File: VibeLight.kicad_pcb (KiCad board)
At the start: 2 copper layers, 61.1 x 36.9 mm, 17 parts, among them SW1 SW_Push, SW2 SW_Push, U2 ADXL343, U3 BL652, U4 LK112M33TR

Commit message: started work on pcb layout
started work on pcb layout
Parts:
- added C5: C, Capacitor_SMD:C_0603_1608Metric_Pad1.08x0.95mm_HandSolder, F.Cu at (77.1, 43.2)
- added C6: C, Capacitor_SMD:C_0603_1608Metric_Pad1.08x0.95mm_HandSolder, F.Cu at (70.3, 38.1)
- added C7: C, Capacitor_SMD:C_0603_1608Metric_Pad1.08x0.95mm_HandSolder, F.Cu at (66.9, 40.6)
- added D1: LED, LED_SMD:LED_0603_1608Metric_Pad1.05x0.95mm_HandSolder, F.Cu at (59.3, 48.3)
- added Mic1: Here for custom footprint, MEMS_Mic_SMD:Mic_SMD_0603_1608Metric, F.Cu at (78.6, 38.6)
- added R3: R, Resistor_SMD:R_0603_1608Metric_Pad0.98x0.95mm_HandSolder, F.Cu at (46.6, 30.5)
- added R4: R, Resistor_SMD:R_0603_1608Metric_Pad0.98x0.95mm_HandSolder, F.Cu at (52.4, 30.5)
- added R5: R, Resistor_SMD:R_0603_1608Metric_Pad0.98x0.95mm_HandSolder, F.Cu at (70.2, 30.5)
- added R6: R, Resistor_SMD:R_0603_1608Metric_Pad0.98x0.95mm_HandSolder, F.Cu at (72.8, 43.2)
- added U1: AD8603, Package_TO_SOT_SMD:TSOT-23-5, F.Cu at (59.6, 37.1)
- RV3: value Intensity Dial -> Sens Dial
- moved C3 48.7 mm to (28.1, 48.6), turned to -90 degrees
- moved PWR_REG1 46.7 mm to (27.0, 44.6), turned to 90 degrees
- moved Accel1 46.1 mm to (69.9, 21.3), turned to -90 degrees
- moved SW2 38.8 mm to (33.0, 20.3)
- moved SW1 27.2 mm to (24.9, 20.3)
- moved R2 25.1 mm to (22.8, 40.6), turned to 180 degrees
- moved R1 20.3 mm to (27.1, 40.6), turned to 180 degrees
- moved RV3 14.7 mm to (66.0, 47.2), turned to 90 degrees
- moved RV2 14.7 mm to (41.7, 20.3)
- moved C1 13.7 mm to (43.2, 43.2)
- moved C4 10.8 mm to (53.3, 18.6)
- moved Temp1 7.65 mm to (56.6, 20.7), turned to 180 degrees
- moved Re1 7.61 mm to (45.7, 48.3), turned to -90 degrees
- moved C2 6.24 mm to (50.8, 48.3), turned to 90 degrees
- moved Re2 5.21 mm to (49.2, 43.2)
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- renumbered U2 to Accel1, U4 to PWR_REG1
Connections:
- net Intensity_Dial renamed /MCU/Intensity_Dial
- Accel1 pad 13: unconnected-(U2-SDA/SDI/SDIO-Pad13) -> /MCU/SCL
- Accel1 pad 14: unconnected-(U2-SCL/SCLK-Pad14) -> Net-(Accel1-SCL/SCLK)
- Accel1 pad 2: Net-(U2-GND-Pad2) -> GND
- Accel1 pad 4: Net-(U2-GND-Pad2) -> GND
- Accel1 pad 5: Net-(U2-GND-Pad2) -> GND
- Accel1 pad 6: +3V3 -> /Audio Input/PWR
- Accel1 pad 7: unconnected-(U2-~{CS}-Pad7) -> /Audio Input/PWR
- Accel1 pad 8: /ACCEL_INT1 -> /MCU/ACC_INT1
- Accel1 pad 9: /ACCEL_INT2 -> /MCU/ACC_INT2
- C4 pad 1: +3V3 -> /Audio Input/PWR
- PWR_REG1 pad 4: +3V3 -> /Audio Input/PWR
- R1 pad 1: Battery -> /Audio Input/PWR
- RV2 pad 1: +3V3 -> /Audio Input/PWR
- RV2 pad 3: /BATT+ -> GND
- RV3 pad 1: unconnected-(RV3-Pad1) -> /Audio Input/RAW
- RV3 pad 2: /Audio Input/Inverting Input -> Net-(U1--)
- RV3 pad 3: unconnected-(RV3-Pad3) -> GND
- SW1 pad 1: /BATT+ -> /MCU/SW1
- SW1 pad 2: unconnected-(SW1-Pad2) -> /Audio Input/PWR
- SW2 pad 1: /BATT+ -> /MCU/SW2
- SW2 pad 2: unconnected-(SW2-Pad2) -> /Audio Input/PWR
- Temp1 pad 1: unconnected-(Temp1-SDA-Pad1) -> Net-(Accel1-SCL/SCLK)
- Temp1 pad 2: unconnected-(Temp1-SCL-Pad2) -> /MCU/SCL
- Temp1 pad 3: +3V3 -> /Audio Input/PWR
- U3 pad 10: unconnected-(U3-SIO_16-Pad10) -> /MCU/SW2
- U3 pad 2: unconnected-(U3-SIO_24-Pad2) -> /MCU/ACC_INT1
- U3 pad 20: /MCU/Batt_Meas -> unconnected-(U3-SIO_05/AIN3-Pad20)
- U3 pad 22: Audio_RAW -> /Audio Input/RAW
- U3 pad 23: /MCU/Audio_FIL -> /Audio Input/FIL
- U3 pad 26: unconnected-(U3-VDD-Pad26) -> /Audio Input/PWR
- U3 pad 29: unconnected-(U3-SIO_15-Pad29) -> /MCU/SW1
- U3 pad 3: unconnected-(U3-SIO_23-Pad3) -> /MCU/ACC_INT2
- U3 pad 36: unconnected-(U3-SIO_27-Pad36) -> /MCU/LED_CNTRL
- U3 pad 38: unconnected-(U3-SIO_25-Pad38) -> /MCU/Batt_Meas
- U3 pad 4: unconnected-(U3-SIO_22-Pad4) -> /MCU/OPT_INT
- U3 pad 5: /MCU/SWDIO -> /MCU/SCL
- U3 pad 6: /MCU/SWCLK -> /MCU/SCL
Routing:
- net /Audio Input/RAW: track 0.00 -> 54.3 mm
- net /MCU/Intensity_Dial: track 29.5 -> 0.00 mm, vias 2 -> 0
- net /Audio Input/FIL: track 0.00 -> 14.1 mm
- net Net-(U1--): track 0.00 -> 12.5 mm
- net Net-(U1-+): track 0.00 -> 12.2 mm, vias 0 -> 2
- net Net-(C1-Pad2): track 0.00 -> 8.50 mm
- net /MCU/Batt_Meas: track 0.00 -> 5.75 mm
- net /Audio Input/PWR: track 0.00 -> 5.71 mm
- net Net-(C7-Pad2): track 0.00 -> 5.17 mm
- net /BATT+: track 0.00 -> 4.19 mm
- net Net-(D1-A): track 0.00 -> 3.59 mm
- net Net-(PWR_REG1-Bypass): track 0.00 -> 2.14 mm
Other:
- board text added: "LIGHT"

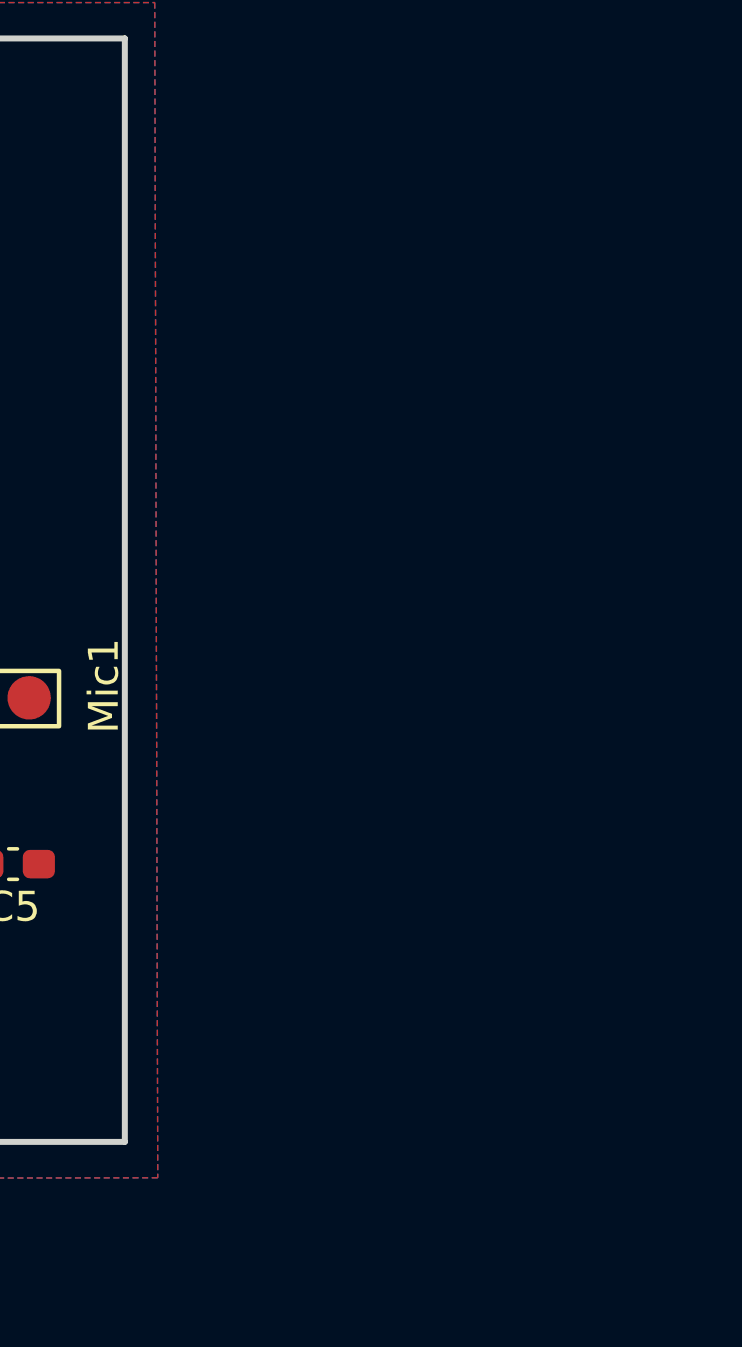
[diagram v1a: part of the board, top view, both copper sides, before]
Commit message: added OPT and JST footprints
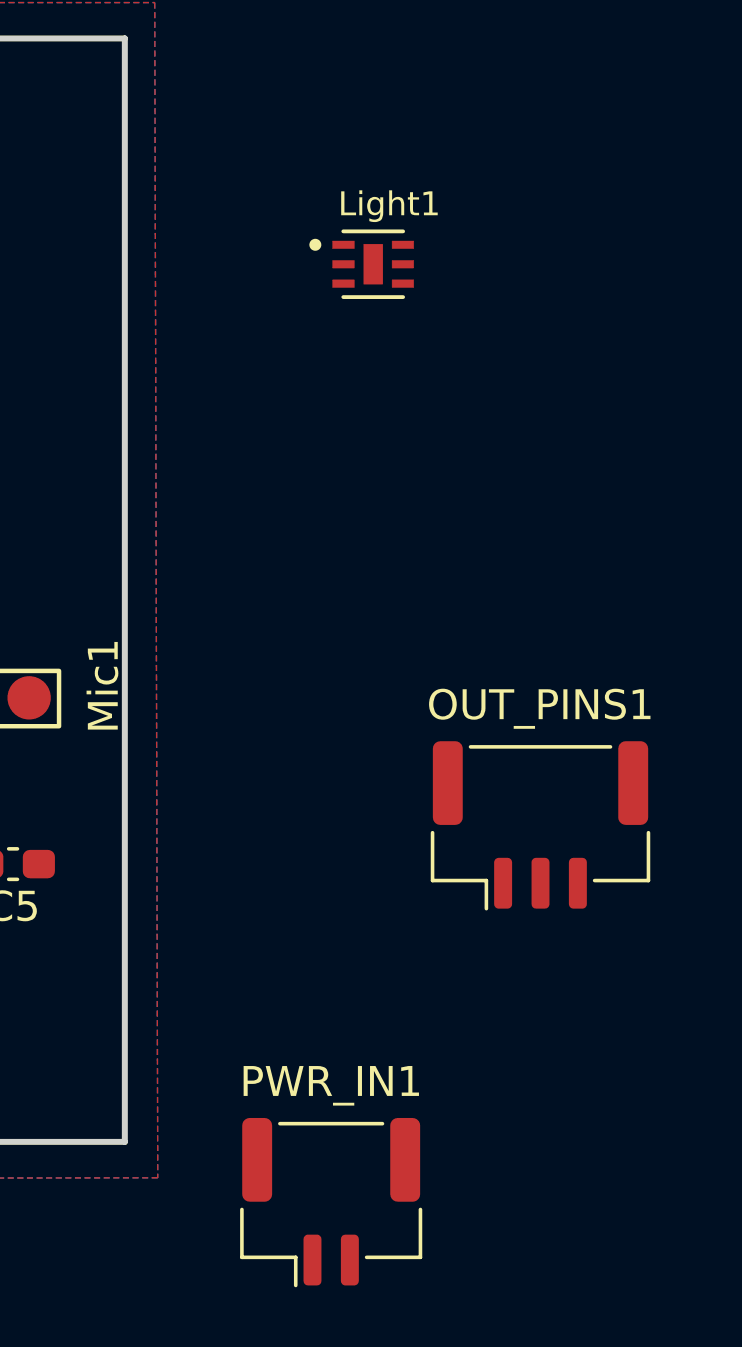
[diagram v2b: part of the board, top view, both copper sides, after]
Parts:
- added Light1: OPT3002-ALS, OP3002:SON65P200X200X65-7N, F.Cu at (89.1, 23.1)
- added OUT_PINS1: Conn_01x03_Pin, Connector_JST:JST_GH_BM03B-GHS-TBT_1x03-1MP_P1.25mm_Vertical, F.Cu at (94.7, 41.9)
- added PWR_IN1: Conn_01x02, Connector_JST:JST_GH_BM02B-GHS-TBT_1x02-1MP_P1.25mm_Vertical, F.Cu at (87.7, 54.5)

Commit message: completed rev1 of PCB layout
need to double check components and other elements, connections, and add values
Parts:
- removed Mic1: Here for custom footprint, MEMS_Mic_SMD:Mic_SMD_0603_1608Metric
- added U2: SPV08A0LR5H-1, MEMS_Mic_SMD:SPV08A0LR5H-1, F.Cu at (77.4, 37.5)
- moved PWR_IN1 63.2 mm to (25.0, 46.4), turned to 90 degrees
- moved OUT_PINS1 27.9 mm to (76.0, 21.2), turned to -90 degrees
- moved Light1 15.0 mm to (77.0, 32.0), turned to 90 degrees
- moved R4 11.4 mm to (41.0, 30.5), turned to 90 degrees
- moved R3 7.63 mm to (39.0, 30.4), turned to 90 degrees
- moved R5 7.23 mm to (77.0, 28.0), turned to -90 degrees
- moved C3 7.01 mm to (35.1, 48.6)
- moved PWR_REG1 7.01 mm to (34.0, 44.6)
- moved R2 7.01 mm to (29.8, 40.6)
- moved R1 7.01 mm to (34.1, 40.6)
- moved Accel1 6.07 mm to (64.0, 20.0)
- moved C4 2.66 mm to (51.0, 19.8)
- moved Temp1 2.66 mm to (54.2, 21.9)
- moved U1 1.85 mm to (59.6, 39.0)
- turned RV2 to -90 degrees
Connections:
- Accel1 pad 13: /MCU/SCL -> /MCU/SDA
- Accel1 pad 14: Net-(Accel1-SCL/SCLK) -> /MCU/SCL
- Light1 pad 6: Net-(Accel1-SCL/SCLK) -> /MCU/SDA
- R3 pad 2: unconnected-(R3-Pad2) -> /MCU/SCL
- R4 pad 2: unconnected-(R4-Pad2) -> /MCU/SDA
- Temp1 pad 1: Net-(Accel1-SCL/SCLK) -> /MCU/SDA
- U3 pad 10: /MCU/SW2 -> unconnected-(U3-SIO_16-Pad10)
- U3 pad 17: unconnected-(U3-SIO_08-Pad17) -> /MCU/ACC_INT1
- U3 pad 18: unconnected-(U3-SIO_07-Pad18) -> /MCU/ACC_INT2
- U3 pad 19: unconnected-(U3-SIO_06-Pad19) -> /MCU/OPT_INT
- U3 pad 2: /MCU/ACC_INT1 -> /MCU/SW1
- U3 pad 21: /MCU/Intensity_Dial -> unconnected-(U3-SIO_04/AIN2-Pad21)
- U3 pad 29: /MCU/SW1 -> unconnected-(U3-SIO_15-Pad29)
- U3 pad 3: /MCU/ACC_INT2 -> /MCU/SW2
- U3 pad 36: /MCU/LED_CNTRL -> unconnected-(U3-SIO_27-Pad36)
- U3 pad 4: /MCU/OPT_INT -> /MCU/Intensity_Dial
- U3 pad 5: /MCU/SCL -> /MCU/SDA
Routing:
- net /Audio Input/PWR: track 5.71 -> 166.4 mm, vias 0 -> 2
- net /MCU/SCL: track 0.00 -> 105.6 mm, vias 0 -> 8
- net /MCU/SDA: track 0.00 -> 94.6 mm, vias 0 -> 8
- net /MCU/OPT_INT: track 0.00 -> 44.6 mm, vias 0 -> 2
- net /MCU/ACC_INT2: track 0.00 -> 32.7 mm, vias 0 -> 2
- net /MCU/ACC_INT1: track 0.00 -> 31.3 mm, vias 0 -> 2
- net /MCU/Intensity_Dial: track 0.00 -> 19.7 mm
- net GND: track 0.00 -> 12.1 mm, vias 0 -> 2
- net /BATT+: track 4.19 -> 9.81 mm
- net /Audio Input/MEMS Mic/2_OUT: track 0.00 -> 5.14 mm
- net /Audio Input/RAW: track 54.3 -> 49.9 mm, vias 0 -> 2
- net /MCU/Batt_Meas: track 5.75 -> 9.03 mm
- net Net-(U1-+): track 12.2 -> 14.6 mm
- net /Audio Input/FIL: track 14.1 -> 15.6 mm, vias 0 -> 2
- net Net-(U1--): track 12.5 -> 12.0 mm
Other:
- board text removed: "LIGHT"

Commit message: Changes from DR call
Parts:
- moved PWR_IN1 62.2 mm to (84.8, 29.1), turned to -90 degrees
- moved PWR_REG1 53.7 mm to (87.2, 37.2)
- moved C3 53.7 mm to (88.3, 41.2)
- moved Light1 21.4 mm to (58.0, 22.0), turned to 180 degrees
- moved R1 9.11 mm to (25.2, 42.7), turned to 0 degrees
- moved OUT_PINS1 9.04 mm to (85.0, 20.4)
- moved C1 5.86 mm to (46.6, 47.9)
- moved C2 5.42 mm to (46.7, 44.7), turned to 180 degrees
- moved Accel1 5.38 mm to (63.9, 25.4)
- moved R2 4.72 mm to (25.1, 41.1)
- moved C4 2.52 mm to (52.2, 22.0), turned to -90 degrees
- moved Re2 2.51 mm to (46.7, 43.2)
- moved Re1 2.17 mm to (46.7, 46.3), turned to 180 degrees
- moved U1 0.71 mm to (59.1, 39.5)
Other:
- board size 61.1 x 36.9 mm -> 52.5 x 20.9 mm

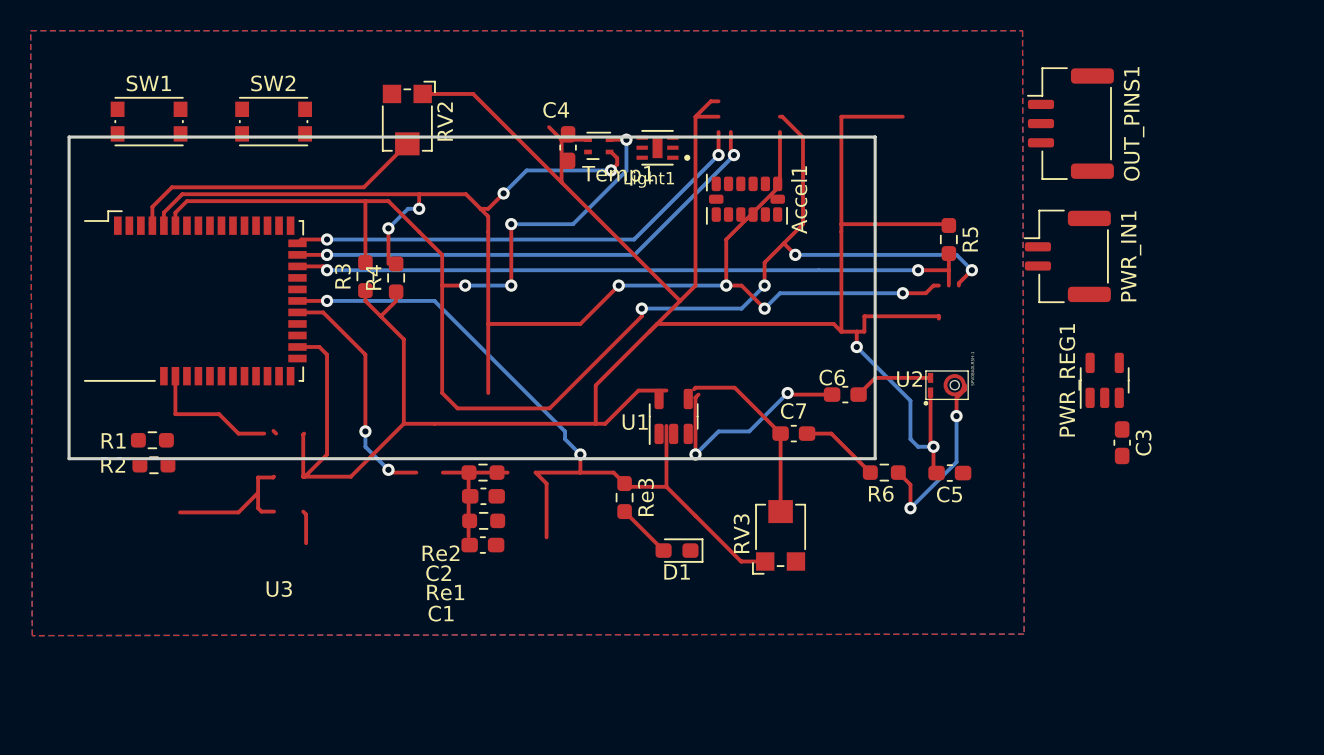
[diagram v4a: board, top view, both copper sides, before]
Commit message: pcB rev2
need to fix reference texts on PCB, figure out MEMs mic wiring
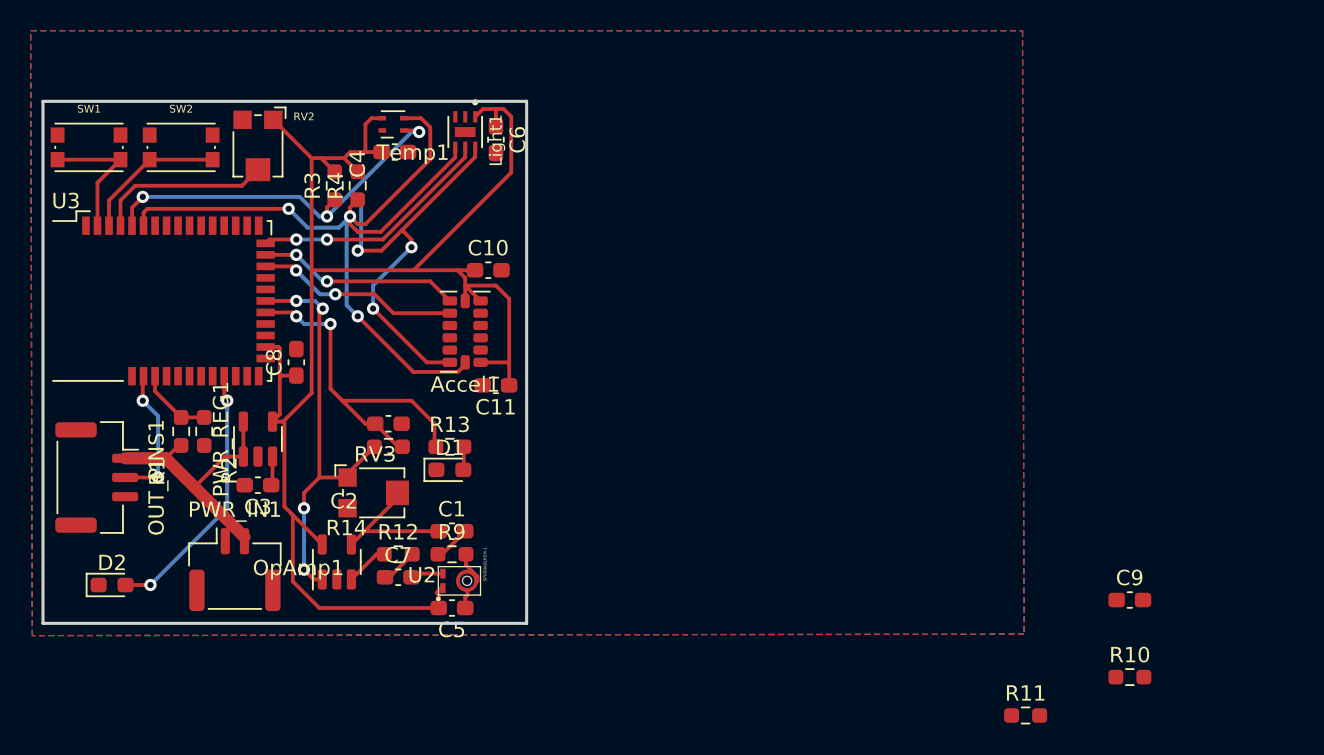
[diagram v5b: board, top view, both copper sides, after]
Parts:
- removed R5, R6: R, Resistor_SMD:R_0603_1608Metric_Pad0.98x0.95mm_HandSolder
- removed Re1: xR, Resistor_SMD:R_0603_1608Metric_Pad0.98x0.95mm_HandSolder
- added C10: 1 uF, Capacitor_SMD:C_0603_1608Metric_Pad1.08x0.95mm_HandSolder, F.Cu at (47.0, 30.0)
- added C11: 100nF, Capacitor_SMD:C_0603_1608Metric_Pad1.08x0.95mm_HandSolder, F.Cu at (47.5, 37.5)
- added C8: 100nF, Capacitor_SMD:C_0603_1608Metric_Pad1.08x0.95mm_HandSolder, F.Cu at (34.5, 36.0)
- added C9: 1uF, Capacitor_SMD:C_0603_1608Metric_Pad1.08x0.95mm_HandSolder, F.Cu at (88.8, 51.5)
- added D2: LED, LED_SMD:LED_0603_1608Metric_Pad1.05x0.95mm_HandSolder, F.Cu at (22.5, 50.5)
- added R10: 10K, Resistor_SMD:R_0603_1608Metric_Pad0.98x0.95mm_HandSolder, F.Cu at (88.8, 56.5)
- added R11: 10K, Resistor_SMD:R_0603_1608Metric_Pad0.98x0.95mm_HandSolder, F.Cu at (82.0, 59.0)
- added R12: 10K, Resistor_SMD:R_0603_1608Metric_Pad0.98x0.95mm_HandSolder, F.Cu at (41.1, 48.5)
- added R9: R, Resistor_SMD:R_0603_1608Metric_Pad0.98x0.95mm_HandSolder, F.Cu at (44.6, 48.5)
- C1: value yC -> C
- C2: value yC -> 1 uF
- C5: value C -> 100 nF
- C6: value C -> 100nF
- C7: value C -> 4.7uF
- OUT_PINS1: footprint Connector_JST:JST_GH_BM03B-GHS-TBT_1x03-1MP_P1.25mm_Vertical -> Connector_JST:JST_GH_SM03B-GHS-TB_1x03-1MP_P1.25mm_Horizontal
- PWR_IN1: footprint Connector_JST:JST_GH_BM02B-GHS-TBT_1x02-1MP_P1.25mm_Vertical -> Connector_JST:JST_GH_SM02B-GHS-TB_1x02-1MP_P1.25mm_Horizontal
- R14: renamed from Re2; value zR -> 620R
- R3, R4: value R -> 4.7K
- moved OUT_PINS1 67.5 mm to (21.5, 43.5)
- moved PWR_IN1 58.0 mm to (30.5, 49.5), turned to 0 degrees
- moved C3 56.4 mm to (32.0, 44.0), turned to 180 degrees
- moved PWR_REG1 55.3 mm to (32.0, 41.0)
- moved U2 34.2 mm to (45.6, 50.2)
- moved C5 33.6 mm to (44.6, 52.0)
- moved C6 28.2 mm to (47.5, 21.5), turned to -90 degrees
- moved C7 27.4 mm to (41.1, 50.0)
- moved RV3 26.5 mm to (39.6, 44.5), turned to 0 degrees
- moved OpAmp1 23.9 mm to (37.1, 49.0)
- moved Accel1 20.3 mm to (45.5, 34.0), turned to 180 degrees
- moved D1 15.7 mm to (44.5, 43.0), turned to 0 degrees
- moved Temp1 13.5 mm to (40.8, 20.5)
- moved Light1 12.6 mm to (45.5, 21.0), turned to -90 degrees
- moved R13 11.9 mm to (44.5, 41.5), turned to 0 degrees
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- renumbered U1 to OpAmp1, Re3 to R13
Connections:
- Accel1 pad 1: unconnected-(Accel1-Vdd_I/O-Pad1) -> +3V3
- Accel1 pad 12: unconnected-(Accel1-SDO/ADDR-Pad12) -> GND
- Accel1 pad 13: /MCU/SDA -> /SDA
- Accel1 pad 14: /MCU/SCL -> /SCL
- Accel1 pad 6: /Audio Input/PWR -> +3V3
- Accel1 pad 7: /Audio Input/PWR -> +3V3
- C1 pad 1: /Audio Input/FIL -> Net-(OpAmp1--)
- C2 pad 2: /Audio Input/RAW -> /Audio Input/FIL
- C4 pad 1: /Audio Input/PWR -> +3V3
- C5 pad 2: /Audio Input/PWR -> +3V3
- C6 pad 1: Net-(U1-+) -> +3V3
- C6 pad 2: /Audio Input/MEMS Mic/2_OUT -> GND
- C7 pad 1: Net-(U1--) -> Net-(C7-Pad1)
- C7 pad 2: Net-(C7-Pad2) -> /Audio Input/MEMS Mic/2_OUT
- Light1 pad 1: /Audio Input/PWR -> +3V3
- Light1 pad 4: /MCU/SCL -> /SCL
- Light1 pad 6: /MCU/SDA -> /SDA
- OUT_PINS1 pad 1: /Audio Input/PWR -> /BATT+
- OUT_PINS1 pad 2: /MCU/LED_CNTRL -> /CNTRL
- OpAmp1 pad 3: Net-(U1-+) -> Net-(OpAmp1-+)
- OpAmp1 pad 4: Net-(U1--) -> Net-(OpAmp1--)
- OpAmp1 pad 5: /Audio Input/PWR -> +3V3
- PWR_REG1 pad 4: /Audio Input/PWR -> +3V3
- R1 pad 1: /Audio Input/PWR -> /BATT+
- R1 pad 2: /MCU/Batt_Meas -> Net-(U3-SIO_26)
- R13 pad 1: /Audio Input/RAW -> /Audio Input/FIL
- R14 pad 1: Net-(C1-Pad2) -> /Audio Input/RAW
- R14 pad 2: /Audio Input/RAW -> /Audio Input/FIL
- R2 pad 1: /MCU/Batt_Meas -> Net-(U3-SIO_26)
- R3 pad 1: /Audio Input/PWR -> /SDA
- R3 pad 2: /MCU/SCL -> +3V3
- R4 pad 1: /Audio Input/PWR -> /SCL
- R4 pad 2: /MCU/SDA -> +3V3
- RV2 pad 1: /Audio Input/PWR -> +3V3
- RV3 pad 2: Net-(U1--) -> Net-(OpAmp1--)
- SW1 pad 2: /Audio Input/PWR -> GND
- SW2 pad 2: /Audio Input/PWR -> GND
- Temp1 pad 1: /MCU/SDA -> /SDA
- Temp1 pad 2: /MCU/SCL -> /SCL
- Temp1 pad 3: /Audio Input/PWR -> +3V3
- U2 pad VDDA: /Audio Input/PWR -> +3V3
- U3 pad 17: /MCU/ACC_INT1 -> /MCU/OPT_INT
- U3 pad 18: /MCU/ACC_INT2 -> /MCU/ACC_INT1
- U3 pad 19: /MCU/OPT_INT -> /MCU/ACC_INT2
- U3 pad 26: /Audio Input/PWR -> +3V3
- U3 pad 31: unconnected-(U3-SIO_19-Pad31) -> /MCU/BATT_LVL
- U3 pad 37: unconnected-(U3-SIO_26-Pad37) -> Net-(U3-SIO_26)
- U3 pad 38: /MCU/Batt_Meas -> /CNTRL
- U3 pad 5: /MCU/SDA -> /SDA
- U3 pad 6: /MCU/SCL -> /SCL
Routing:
- net /Audio Input/PWR: track 166.4 -> 0.00 mm, vias 2 -> 0
- net +3V3: track 0.00 -> 106.4 mm
- net /MCU/SCL: track 105.6 -> 0.00 mm, vias 8 -> 0
- net /MCU/SDA: track 94.6 -> 0.00 mm, vias 8 -> 0
- net /SCL: track 0.00 -> 53.7 mm, vias 0 -> 3
- net /SDA: track 0.00 -> 53.1 mm, vias 0 -> 6
- net /MCU/OPT_INT: track 44.6 -> 16.0 mm
- net /Audio Input/RAW: track 49.9 -> 27.5 mm, vias 2 -> 4
- net /MCU/ACC_INT2: track 32.7 -> 13.3 mm
- net /MCU/ACC_INT1: track 31.3 -> 13.2 mm
- net /MCU/BATT_LVL: track 0.00 -> 17.4 mm, vias 0 -> 2
- net Net-(U1-+): track 14.6 -> 0.00 mm, vias 2 -> 0
- net Net-(U1--): track 12.0 -> 0.00 mm
- net /MCU/SW2: track 0.00 -> 9.50 mm
- net Net-(OpAmp1--): track 0.00 -> 9.43 mm
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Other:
- board size 52.5 x 20.9 mm -> 31.5 x 34 mm

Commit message: slight layout changes, nothing big
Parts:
- R12: value 10K -> 4.7K
- R13: value xR -> 60R
- moved C6 7.43 mm to (43.3, 27.6), turned to 180 degrees
- moved Light1 4.92 mm to (43.8, 25.6), turned to 180 degrees
- moved Accel1 2.92 mm to (42.6, 34.6)
- moved C10 2.92 mm to (44.1, 30.6)
- moved C11 2.92 mm to (44.6, 38.1)
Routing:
- net +3V3: track 106.4 -> 94.9 mm
- net /SCL: track 53.7 -> 45.1 mm
- net /SDA: track 53.1 -> 44.8 mm, vias 6 -> 5
- net /MCU/OPT_INT: track 16.0 -> 11.4 mm
- net /MCU/ACC_INT2: track 13.3 -> 10.6 mm
- net /MCU/ACC_INT1: track 13.2 -> 10.6 mm
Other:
- board size 31.5 x 34 mm -> 29 x 34 mm
